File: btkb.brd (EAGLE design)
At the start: 100 x 80 mm, 1 part

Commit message: I added the RN-42 to the schematic! lol!
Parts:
- removed JP1: (no value), jumper:JP4
- added U$1: BLUETOOTH-RN41", SparkFun-RF:RN41
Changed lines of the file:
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@@
 <layer number="48" name="Document" color="7" fill="1" visible="yes" active="yes"/>
 <layer number="49" name="Reference" color="7" fill="1" visible="yes" active="yes"/>
+<layer number="50" name="dxf" color="7" fill="1" visible="no" active="no"/>
 <layer number="51" name="tDocu" color="7" fill="1" visible="yes" active="yes"/>
 <layer number="52" name="bDocu" color="7" fill="1" visible="yes" active="yes"/>
+<layer number="53" name="tGND_GNDA" color="7" fill="9" visible="no" active="no"/>
+<layer number="54" name="bGND_GNDA" color="1" fill="9" visible="no" active="no"/>
+<layer number="56" name="wert" color="7" fill="1" visible="no" active="no"/>
+<layer number="57" name="tCAD" color="7" fill="1" visible="no" active="no"/>
 <layer number="90" name="Modules" color="5" fill="1" visible="no" active="no"/>
 <layer number="91" name="Nets" color="2" fill="1" visible="no" active="no"/>
@@
 <layer number="97" name="Info" color="7" fill="1" visible="no" active="no"/>
 <layer number="98" name="Guide" color="6" fill="1" visible="no" active="no"/>
+<layer number="99" name="SpiceOrder" color="7" fill="1" visible="no" active="no"/>
+<layer number="100" name="Muster" color="7" fill="1" visible="no" active="no"/>
+<layer number="101" name="Patch_Top" color="12" fill="4" visible="yes" active="yes"/>
+<layer number="102" name="Vscore" color="7" fill="1" visible="yes" active="yes"/>
+<layer number="103" name="tMap" color="7" fill="1" visible="yes" active="yes"/>
+<layer number="104" name="Name" color="16" fill="1" visible="yes" active="yes"/>
+<layer number="105" name="tPlate" color="7" fill="1" visible="yes" active="yes"/>
+<layer number="106" name="bPlate" color="7" fill="1" visible="yes" active="yes"/>
+<layer number="107" name="Crop" color="7" fill="1" visible="yes" active="yes"/>
+<layer number="108" name="tplace-old" color="10" fill="1" visible="yes" active="yes"/>
+<layer number="109" name="ref-old" color="11" fill="1" visible="yes" active="yes"/>
+<layer number="110" name="fp0" color="7" fill="1" visible="yes" active="yes"/>
+<layer number="111" name="LPC17xx" color="7" fill="1" visible="yes" active="yes"/>
+<layer number="112" name="tSilk" color="7" fill="1" visible="yes" active="yes"/>
+<layer number="113" name="IDFDebug" color="4" fill="1" visible="yes" active="yes"/>
+<layer number="116" name="Patch_BOT" color="9" fill="4" visible="yes" active="yes"/>
+<layer number="121" name="_tsilk" color="7" fill="1" visible="yes" active="yes"/>
+<layer number="122" name="_bsilk" color="7" fill="1" visible="yes" active="yes"/>
+<layer number="123" name="tTestmark" color="7" fill="1" visible="yes" active="yes"/>
+<layer number="124" name="bTestmark" color="7" fill="1" visible="yes" active="yes"/>
+<layer number="125" name="_tNames" color="7" fill="1" visible="yes" active="yes"/>
+<layer number="126" name="_bNames" color="7" fill="1" visible="yes" active="yes"/>
+<layer number="127" name="_tValues" color="7" fill="1" visible="yes" active="yes"/>
+<layer number="128" name="_bValues" color="7" fill="1" visible="yes" active="yes"/>
+<layer number="131" name="tAdjust" color="7" fill="1" visible="yes" active="yes"/>
+<layer number="132" name="bAdjust" color="7" fill="1" visible="yes" active="yes"/>
+<layer number="144" name="Drill_legend" color="7" fill="1" visible="yes" active="yes"/>
+<layer number="150" name="Notes" color="7" fill="1" visible="yes" active="yes"/>
+<layer number="151" name="HeatSink" color="7" fill="1" visible="yes" active="yes"/>
+<layer number="152" name="_bDocu" color="7" fill="1" visible="yes" active="yes"/>
+<layer number="153" name="FabDoc1" color="7" fill="1" visible="yes" active="yes"/>
+<layer number="154" name="FabDoc2" color="7" fill="1" visible="yes" active="yes"/>
+<layer number="155" name="FabDoc3" color="7" fill="1" visible="yes" active="yes"/>
+<layer number="199" name="Contour" color="7" fill="1" visible="yes" active="yes"/>
+<layer number="200" name="200bmp" color="1" fill="10" visible="yes" active="yes"/>
+<layer number="201" name="201bmp" color="2" fill="10" visible="yes" active="yes"/>
+<layer number="202" name="202bmp" color="3" fill="10" visible="yes" active="yes"/>
+<layer number="203" name="203bmp" color="4" fill="10" visible="yes" active="yes"/>
+<layer number="204" name="204bmp" color="5" fill="10" visible="yes" active="yes"/>
+<layer number="205" name="205bmp" color="6" fill="10" visible="yes" active="yes"/>
+<layer number="206" name="206bmp" color="7" fill="10" visible="yes" active="yes"/>
+<layer number="207" name="207bmp" color="8" fill="10" visible="yes" active="yes"/>
+<layer number="208" name="208bmp" color="9" fill="10" visible="yes" active="yes"/>
+<layer number="209" name="209bmp" color="7" fill="1" visible="yes" active="yes"/>
+<layer number="210" name="210bmp" color="7" fill="1" visible="yes" active="yes"/>
+<layer number="211" name="211bmp" color="7" fill="1" visible="yes" active="yes"/>
+<layer number="212" name="212bmp" color="7" fill="1" visible="yes" active="yes"/>
+<layer number="213" name="213bmp" color="7" fill="1" visible="yes" active="yes"/>
+<layer number="214" name="214bmp" color="7" fill="1" visible="yes" active="yes"/>
+<layer number="215" name="215bmp" color="7" fill="1" visible="yes" active="yes"/>
+<layer number="216" name="216bmp" color="7" fill="1" visible="yes" active="yes"/>
+<layer number="217" name="217bmp" color="18" fill="1" visible="no" active="no"/>
+<layer number="218" name="218bmp" color="19" fill="1" visible="no" active="no"/>
+<layer number="219" name="219bmp" color="20" fill="1" visible="no" active="no"/>
+<layer number="220" name="220bmp" color="21" fill="1" visible="no" active="no"/>
+<layer number="221" name="221bmp" color="22" fill="1" visible="no" active="no"/>
+<layer number="222" name="222bmp" color="23" fill="1" visible="no" active="no"/>
+<layer number="223" name="223bmp" color="24" fill="1" visible="no" active="no"/>
+<layer number="224" name="224bmp" color="25" fill="1" visible="no" active="no"/>
+<layer number="248" name="Housing" color="7" fill="1" visible="yes" active="yes"/>
+<layer number="249" name="Edge" color="7" fill="1" visible="yes" active="yes"/>
+<layer number="250" name="Descript" color="3" fill="1" visible="no" active="no"/>
+<layer number="251" name="SMDround" color="12" fill="11" visible="no" active="no"/>
+<layer number="254" name="cooling" color="7" fill="1" visible="yes" active="yes"/>
 </layers>
 <board>
@@
 </autorouter>
 <elements>
-<element name="JP1" library="jumper" package="JP4" value="" x="10.16" y="73.66"/>
+<element name="U$1" library="SparkFun-RF" package="RN41" value="BLUETOOTH-RN41&quot;" x="16.51" y="-7.62"/>
 </elements>
 <signals>

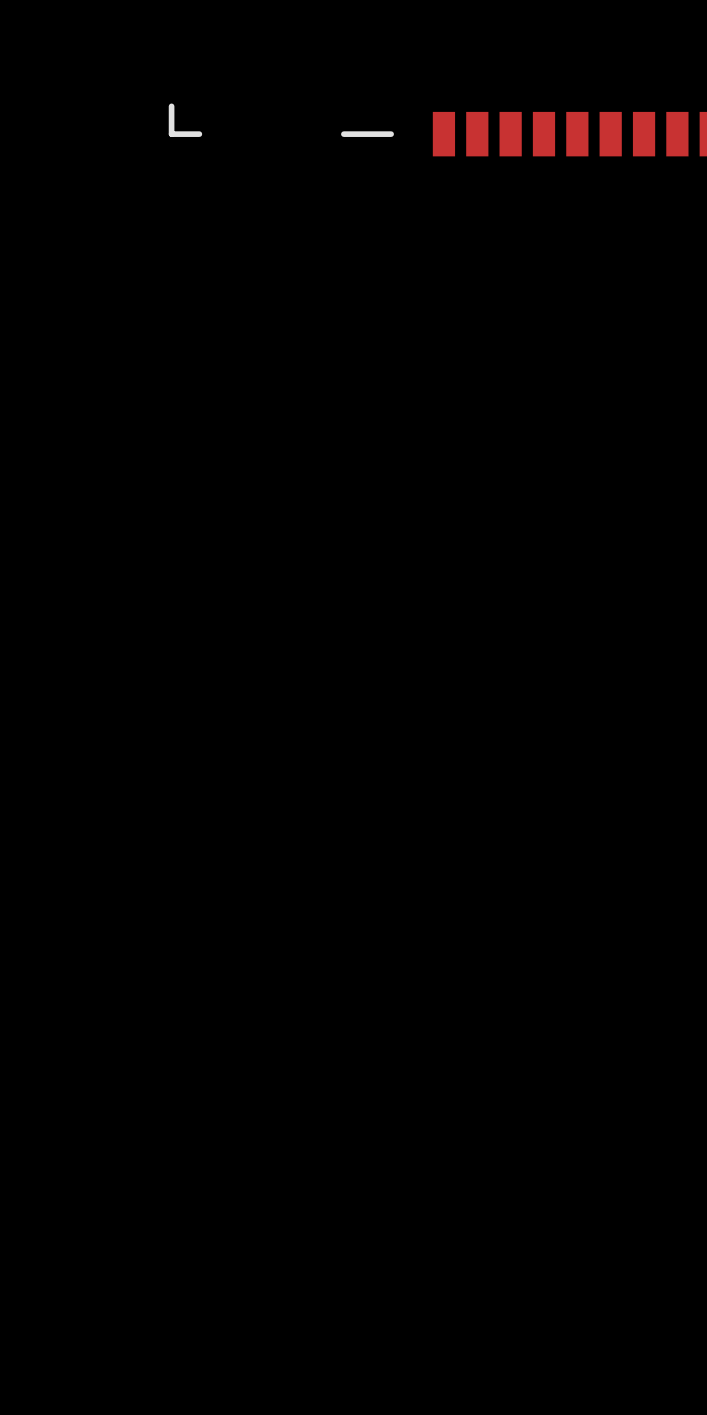
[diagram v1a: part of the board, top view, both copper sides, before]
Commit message: Added components copy pasta'ed from other schematics
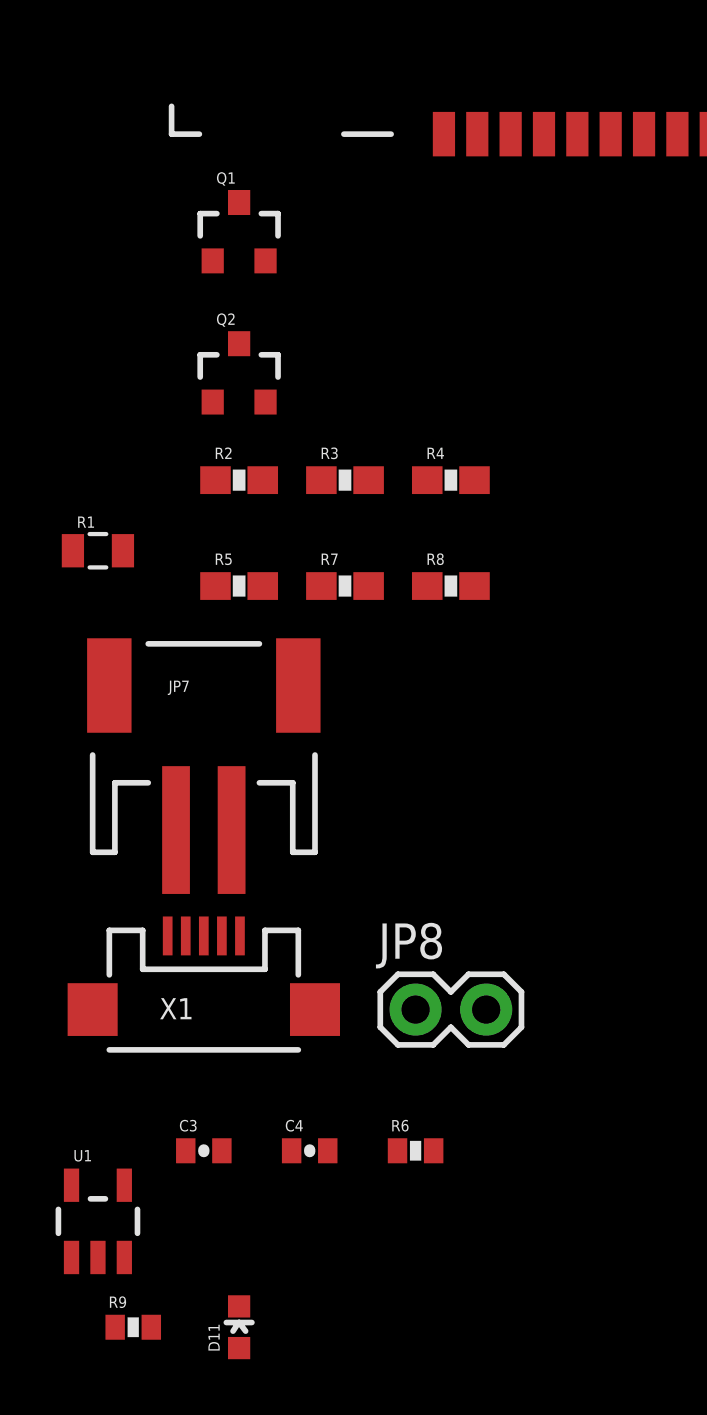
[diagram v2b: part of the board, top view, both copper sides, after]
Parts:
- added C3, C4: 4.7uF, SparkFun:0402-CAP
- added D11: RED, SparkFun:LED-0603
- added JP7: LiPo Battery, SparkFun:JST-2-SMD
- added JP8: (no value), SparkFun:1X02
- added Q1, Q2: MOSFET-NCHANNELSMD, SparkFun:SOT23-3
- added R1: 10k, SparkFun-Resistors:0805
- added R2, R3, R4, R5, R7, R8: 10K, SparkFun:0603-RES
- added R6: 330, SparkFun:0402-RES
- added R9: 2K, SparkFun:0402-RES
- added U1: MCP73831, SparkFun:SOT23-5
- added X1: Micro USB, SparkFun:USB-MICROB
- IC1: value BLUETOOTH-RN41" -> BLUETOOTH-RN42 HID
- renumbered U$1 to IC1
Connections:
- new net 3.3V: Q1.1, Q2.1, R3.1, R7.1
- new net CTS: R2.1
- new net CTS_5V: R2.2
- new net GND: C3.2, C4.2, IC1.1, IC1.12, IC1.28, IC1.29, JP7.1, JP8.1, R9.2, U1.2, X1.GND
- new net N$1: IC1.13
- new net N$10: IC1.21
- new net N$11: IC1.11
- new net N$12: D11.A, R6.1
- new net N$2: IC1.14
- new net N$3: IC1.15
- new net N$4: IC1.16
- new net N$5: IC1.18
- new net N$6: IC1.17
- new net N$8: IC1.19
- new net N$9: IC1.22
- new net PROG: R9.1, U1.5
- new net RTS: Q2.2, R7.2
- new net RTS_5V: Q2.3, R8.2
- new net RX: R5.1
- new net RX_5V: R5.2
- new net STAT: D11.C, U1.1
- new net TX: Q1.2, R3.2
- new net TX_5V: Q1.3, R4.2
- new net VCC: C4.1, JP7.2, JP8.2, R4.1, R8.1, U1.3
- new net VIN: C3.1, R6.2, U1.4, X1.VBUS
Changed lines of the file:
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@@
 <?xml version="1.0" encoding="utf-8"?>
 <!DOCTYPE eagle SYSTEM "eagle.dtd">
-<eagle version="7.4.0">
+<eagle version="6.6.0">
 <drawing>
 <settings>
@@
 <layer number="223" name="223bmp" color="24" fill="1" visible="no" active="no"/>
 <layer number="224" name="224bmp" color="25" fill="1" visible="no" active="no"/>
+<layer number="225" name="225bmp" color="7" fill="1" visible="yes" active="yes"/>
+<layer number="226" name="226bmp" color="7" fill="1" visible="yes" active="yes"/>
+<layer number="227" name="227bmp" color="7" fill="1" visible="yes" active="yes"/>
+<layer number="228" name="228bmp" color="7" fill="1" visible="yes" active="yes"/>
+<layer number="229" name="229bmp" color="7" fill="1" visible="yes" active="yes"/>
+<layer number="230" name="230bmp" color="7" fill="1" visible="yes" active="yes"/>
+<layer number="231" name="231bmp" color="7" fill="1" visible="yes" active="yes"/>
 <layer number="248" name="Housing" color="7" fill="1" visible="yes" active="yes"/>
 <layer number="249" name="Edge" color="7" fill="1" visible="yes" active="yes"/>
@@
 <pass name="Default">
 <param name="RoutingGrid" value="50mil"/>
-<param name="AutoGrid" value="1"/>
-<param name="Efforts" value="0"/>
-<param name="TopRouterVariant" value="1"/>
 <param name="tpViaShape" value="round"/>
-<param name="PrefDir.1" value="a"/>
+<param name="PrefDir.1" value="|"/>
 <param name="PrefDir.2" value="0"/>
 <param name="PrefDir.3" value="0"/>
@@
 <param name="PrefDir.14" value="0"/>
 <param name="PrefDir.15" value="0"/>
-<param name="PrefDir.16" value="a"/>
+<param name="PrefDir.16" value="-"/>
 <param name="cfVia" value="8"/>
 <param name="cfNonPref" value="5"/>
@@
 </autorouter>
 <elements>
-<element name="U$1" library="SparkFun-RF" package="RN41" value="BLUETOOTH-RN41&quot;" x="16.51" y="-7.62"/>
+<element name="IC1" library="SparkFun-RF" package="RN41" value="BLUETOOTH-RN42 HID" x="16.51" y="-7.62"/>
+<element name="Q2" library="SparkFun" package="SOT23-3" value="MOSFET-NCHANNELSMD" x="2.54" y="-22.86"/>
+<element name="R7" library="SparkFun" package="0603-RES" value="10K" x="6.35" y="-30.48"/>
+<element name="R8" library="SparkFun" package="0603-RES" value="10K" x="10.16" y="-30.48"/>
+<element name="R2" library="SparkFun" package="0603-RES" value="10K" x="2.54" y="-26.67"/>
+<element name="Q1" library="SparkFun" package="SOT23-3" value="MOSFET-NCHANNELSMD" x="2.54" y="-17.78"/>
+<element name="R3" library="SparkFun" package="0603-RES" value="10K" x="6.35" y="-26.67"/>
+<element name="R4" library="SparkFun" package="0603-RES" value="10K" x="10.16" y="-26.67"/>
+<element name="R5" library="SparkFun" package="0603-RES" value="10K" x="2.54" y="-30.48"/>
+<element name="R1" library="SparkFun-Resistors" package="0805" value="10k" x="-2.54" y="-29.21">
+<attribute name="PROD_ID" value="RES-09883" x="-2.54" y="-29.21" size="1.778" layer="27" display="off"/>
+</element>
+<element name="D11" library="SparkFun" package="LED-0603" value="RED" x="2.54" y="-57.15"/>
+<element name="R6" library="SparkFun" package="0402-RES" value="330" x="8.89" y="-50.8"/>
+<element name="U1" library="SparkFun" package="SOT23-5" value="MCP73831" x="-2.54" y="-53.34"/>
+<element name="R9" library="SparkFun" package="0402-RES" value="2K" x="-1.27" y="-57.15"/>
+<element name="C3" library="SparkFun" package="0402-CAP" value="4.7uF" x="1.27" y="-50.8"/>
+<element name="C4" library="SparkFun" package="0402-CAP" value="4.7uF" x="5.08" y="-50.8"/>
+<element name="JP7" library="SparkFun" package="JST-2-SMD" value="LiPo Battery" x="1.27" y="-35.56"/>
+<element name="JP8" library="SparkFun" package="1X02" value="" x="8.89" y="-45.72"/>
+<element name="X1" library="SparkFun" package="USB-MICROB" value="Micro USB" x="1.27" y="-45.72"/>
 </elements>
 <signals>
+<signal name="TX">
+<contactref element="Q1" pad="2"/>
+<contactref element="R3" pad="2"/>
+<wire x1="3.49" y1="-18.78" x2="7.2" y2="-26.67" width="0" layer="19" extent="1-1"/>
+</signal>
+<signal name="3.3V">
+<contactref element="R7" pad="1"/>
+<contactref element="Q2" pad="1"/>
+<contactref element="R3" pad="1"/>
+<contactref element="Q1" pad="1"/>
+<wire x1="5.5" y1="-26.67" x2="5.5" y2="-30.48" width="0" layer="19" extent="1-1"/>
+<wire x1="1.59" y1="-23.86" x2="5.5" y2="-26.67" width="0" layer="19" extent="1-1"/>
+<wire x1="1.59" y1="-18.78" x2="1.59" y2="-23.86" width="0" layer="19" extent="1-1"/>
+</signal>
+<signal name="TX_5V">
+<contactref element="Q1" pad="3"/>
+<contactref element="R4" pad="2"/>
+<wire x1="2.54" y1="-16.68" x2="11.01" y2="-26.67" width="0" layer="19" extent="1-1"/>
+</signal>
+<signal name="RX">
+<contactref element="R5" pad="1"/>
+</signal>
+<signal name="RX_5V">
+<contactref element="R5" pad="2"/>
+</signal>
+<signal name="VCC">
+<contactref element="R8" pad="1"/>
+<contactref element="R4" pad="1"/>
+<contactref element="U1" pad="3"/>
+<contactref element="C4" pad="1"/>
+<contactref element="JP8" pad="2"/>
+<contactref element="JP7" pad="2"/>
+<wire x1="4.43" y1="-50.8" x2="-1.59" y2="-54.6401" width="0" layer="19" extent="1-1"/>
+<wire x1="11.43" y1="-45.72" x2="4.43" y2="-50.8" width="0" layer="19" extent="1-1"/>
+<wire x1="2.27" y1="-39.26" x2="11.43" y2="-45.72" width="0" layer="19" extent="1-1"/>
+<wire x1="9.31" y1="-30.48" x2="2.27" y2="-39.26" width="0" layer="19" extent="1-1"/>
+<wire x1="9.31" y1="-26.67" x2="9.31" y2="-30.48" width="0" layer="19" extent="1-1"/>
+</signal>
+<signal name="RTS">
+<contactref element="Q2" pad="2"/>
+<contactref element="R7" pad="2"/>
+<wire x1="3.49" y1="-23.86" x2="7.2" y2="-30.48" width="0" layer="19" extent="1-1"/>
+</signal>
+<signal name="RTS_5V">
+<contactref element="Q2" pad="3"/>
+<contactref element="R8" pad="2"/>
+<wire x1="2.54" y1="-21.76" x2="11.01" y2="-30.48" width="0" layer="19" extent="1-1"/>
+</signal>
+<signal name="CTS">
+<contactref element="R2" pad="1"/>
+</signal>
+<signal name="CTS_5V">
+<contactref element="R2" pad="2"/>
+</signal>
+<signal name="N$1">
+<contactref element="IC1" pad="13"/>
+</signal>
+<signal name="N$2">
+<contactref element="IC1" pad="14"/>
+</signal>
+<signal name="N$3">
+<contactref element="IC1" pad="15"/>
+</signal>
+<signal name="N$4">
+<contactref element="IC1" pad="16"/>
+</signal>
+<signal name="N$5">
+<contactref element="IC1" pad="18"/>
+</signal>
+<signal name="N$6">
+<contactref element="IC1" pad="17"/>
+</signal>
+<signal name="N$8">
+<contactref element="IC1" pad="19"/>
+</signal>
+<signal name="N$9">
+<contactref element="IC1" pad="22"/>
+</signal>
+<signal name="N$10">
+<contactref element="IC1" pad="21"/>
+</signal>
+<signal name="N$11">
+<contactref element="IC1" pad="11"/>
+</signal>
+<signal name="VIN">
+<contactref element="U1" pad="4"/>
+<contactref element="R6" pad="2"/>
+<contactref element="C3" pad="1"/>
+<contactref element="X1" pad="VBUS"/>
+<wire x1="0.62" y1="-50.8" x2="-1.59" y2="-52.0399" width="0" layer="19" extent="1-1"/>
+<wire x1="-0.03" y1="-43.07" x2="0.62" y2="-50.8" width="0" layer="19" extent="1-1"/>
+<wire x1="9.54" y1="-50.8" x2="0.62" y2="-50.8" width="0" layer="19" extent="1-1"/>
+</signal>
+<signal name="GND">
+<contactref element="C4" pad="2"/>
+<contactref element="C3" pad="2"/>
+<contactref element="U1" pad="2"/>
+<contactref element="R9" pad="2"/>
+<contactref element="X1" pad="GND"/>
+<contactref element="JP8" pad="1"/>
+<contactref element="JP7" pad="1"/>
+<contactref element="IC1" pad="1"/>
+<contactref element="IC1" pad="12"/>
+<contactref element="IC1" pad="28"/>
+<contactref element="IC1" pad="29"/>
+<wire x1="-0.62" y1="-57.15" x2="-2.54" y2="-54.6401" width="0" layer="19" extent="1-1"/>
+<wire x1="1.92" y1="-50.8" x2="-2.54" y2="-54.6401" width="0" layer="19" extent="1-1"/>
+<wire x1="5.73" y1="-50.8" x2="1.92" y2="-50.8" width="0" layer="19" extent="1-1"/>
+<wire x1="8.89" y1="-45.72" x2="5.73" y2="-50.8" width="0" layer="19" extent="1-1"/>
+<wire x1="2.57" y1="-43.07" x2="8.89" y2="-45.72" width="0" layer="19" extent="1-1"/>
+<wire x1="0.27" y1="-39.26" x2="2.57" y2="-43.07" width="0" layer="19" extent="1-1"/>
+<wire x1="9.91" y1="-14.22" x2="0.27" y2="-39.26" width="0" layer="19" extent="1-1"/>
+<wire x1="23.11" y1="-14.22" x2="9.91" y2="-14.22" width="0" layer="19" extent="1-1"/>
+<wire x1="25.91" y1="-10.72" x2="23.11" y2="-14.22" width="0" layer="19" extent="1-1"/>
+<wire x1="25.91" y1="-4.52" x2="25.91" y2="-10.72" width="0" layer="19" extent="1-1"/>
+</signal>
+<signal name="N$12">
+<contactref element="D11" pad="A"/>
+<contactref element="R6" pad="1"/>
+<wire x1="8.24" y1="-50.8" x2="2.54" y2="-57.9" width="0" layer="19" extent="1-1"/>
+</signal>
+<signal name="PROG">
+<contactref element="U1" pad="5"/>
+<contactref element="R9" pad="1"/>
+<wire x1="-3.49" y1="-52.0399" x2="-1.92" y2="-57.15" width="0" layer="19" extent="1-1"/>
+</signal>
+<signal name="STAT">
+<contactref element="D11" pad="C"/>
+<contactref element="U1" pad="1"/>
+<wire x1="2.54" y1="-56.4" x2="-3.49" y2="-54.6401" width="0" layer="19" extent="1-1"/>
+</signal>
 </signals>
 </board>
